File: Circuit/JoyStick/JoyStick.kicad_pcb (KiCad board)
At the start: 2 copper layers, 35.8 x 30.7 mm, 0 parts

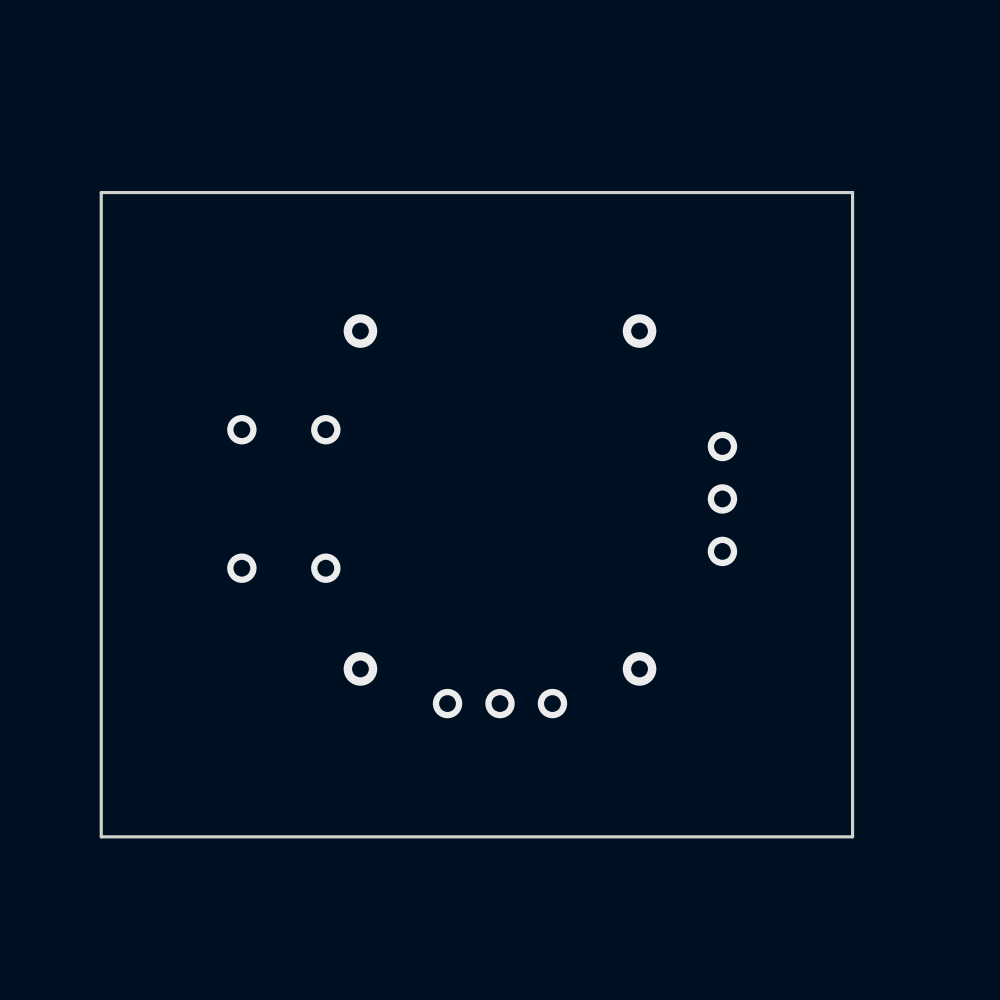
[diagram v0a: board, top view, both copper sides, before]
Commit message: ジョイスティック固定威容の基板外形を円形へ変更
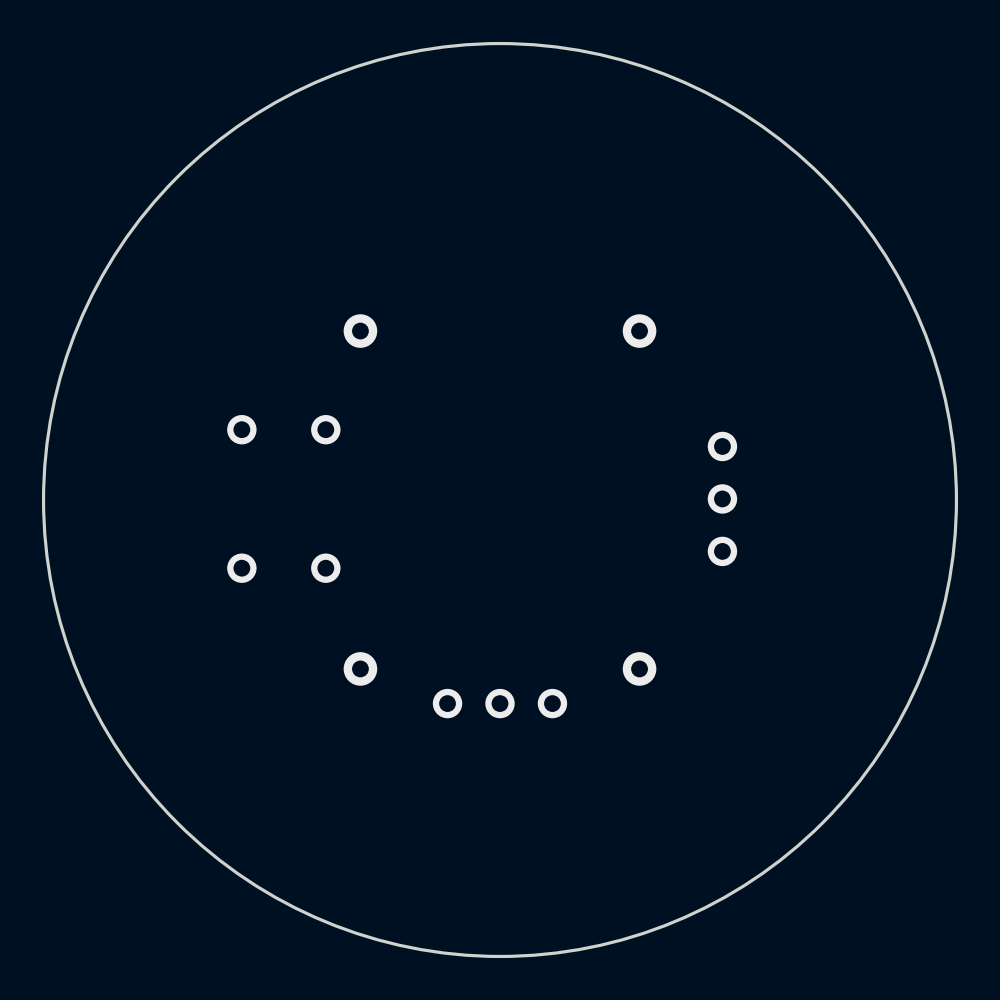
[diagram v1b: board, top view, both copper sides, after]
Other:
- board size 35.8 x 30.7 mm -> 43.5 x 43.5 mm
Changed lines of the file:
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@@
     (area 69.899999 86.399999 106.100001 117.600001)
     (thickness 1.6)
-    (drawings 16)
+    (drawings 26)
     (tracks 14)
     (zones 0)
@@
     (pad_to_mask_clearance 0.2)
     (aux_axis_origin 0 0)
-    (visible_elements FFFFFF7F)
+    (visible_elements 7FFFFFFF)
     (pcbplotparams
       (layerselection 0x01800_00000000)
@@
     (uvia_drill 0.1)
   )
+  (gr_line (start 106 95.5) (end 109.95 95.5) (layer Eco2.User) (width 0.2))
+  (gr_line (start 105.75 100) (end 110.75 100) (layer Eco2.User) (width 0.2))
+  (gr_line (start 105.75 102.75) (end 110.75 102.75) (layer Eco2.User) (width 0.2))
+  (gr_line (start 106 107) (end 110.05 107) (layer Eco2.User) (width 0.2))
+  (gr_line (start 93.5 122.75) (end 93.5 117.5) (layer Eco2.User) (width 0.2))
+  (gr_line (start 90.25 123.2) (end 90.25 117.5) (layer Eco2.User) (width 0.2))
+  (gr_line (start 87.75 123.2) (end 87.75 117.5) (layer Eco2.User) (width 0.2))
+  (gr_line (start 84.5 117.5) (end 84.5 122.75) (layer Eco2.User) (width 0.2))
+  (gr_line (start 70 107) (end 67.95 107) (layer Eco2.User) (width 0.2))
+  (gr_line (start 70 95.5) (end 68.1 95.5) (layer Eco2.User) (width 0.2))
+  (gr_line (start 70 101.5) (end 67.25 101.5) (layer Eco2.User) (width 0.2))
+  (gr_line (start 89 86.5) (end 89 79.7) (layer Eco2.User) (width 0.2))
+  (gr_circle (center 89 101.45) (end 103.75 101.45) (layer Eco1.User) (width 0.2))
+  (gr_circle (center 89 101.45) (end 110.75 101.45) (layer Edge.Cuts) (width 0.15))
   (gr_line (start 89 102.75) (end 105.75 102.75) (angle 90) (layer Eco2.User) (width 0.2))
   (gr_line (start 105.75 100) (end 89 100) (angle 90) (layer Eco2.User) (width 0.2))
@@
   (gr_line (start 78.5 95.5) (end 78.5 107) (angle 90) (layer Eco2.User) (width 0.2))
   (gr_line (start 106 95.5) (end 70 95.5) (angle 90) (layer Eco2.User) (width 0.2))
-  (gr_line (start 105.8 86.8) (end 70 86.8) (angle 90) (layer Edge.Cuts) (width 0.15))
-  (gr_line (start 105.8 117.5) (end 105.8 86.8) (angle 90) (layer Edge.Cuts) (width 0.15))
-  (gr_line (start 70 117.5) (end 105.8 117.5) (angle 90) (layer Edge.Cuts) (width 0.15))
-  (gr_line (start 70 86.8) (end 70 117.5) (angle 90) (layer Edge.Cuts) (width 0.15))
   (via (at 99.6 103.9) (size 1.4) (drill 0.8) (layers F.Cu B.Cu) (net 0))
   (via (at 99.6 101.4) (size 1.4) (drill 0.8) (layers F.Cu B.Cu) (net 0))
